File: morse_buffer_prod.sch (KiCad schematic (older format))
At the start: 105 parts, among them J1 Columns, J2 EXT_SW, J3 Rows, J4 TRIG_OUT, J5 Barrel_Jack_Switch, K1 G5V-1, Q1 MMBT2222A, Q2 MMBT2222A, Q3 NCE30P12S, Q4 MMBT2222A, SW1 M_RST, SW2 BTN, SW3 OUTPUT_SEL, U1 NE555D, U10 74HC138, U11 74HC138, U12 IDT7201LA50TP, U13 MORSE_EEPROM, U14 LENGTH_EEPROM, U15 74HC151, U16 74HC688, U17 74HC221, U18 74HC74, U19 74HC161, U2 NE555D, U20 74HC161, U21 PC817, U3 74HC32, U4 74HC32, U5 74HC14, U6 74HC10, U7 74HC74, U8 74HC74, U9 74HC161

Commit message: Add PS/2 controller
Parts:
- removed C21: 10nF, Capacitor_SMD:C_0603_1608Metric, symbol Device:C
- removed C22: 10uF, Capacitor_THT:CP_Radial_D5.0mm_P2.00mm, symbol Device:CP
- removed D1: TX/WAIT, LED_SMD:LED_0603_1608Metric, symbol Device:LED
- removed J1: Columns, Connector_PinHeader_2.54mm:PinHeader_1x13_P2.54mm_Vertical, symbol Connector:Screw_Terminal_01x13
- removed J3: Rows, Connector_PinHeader_2.54mm:PinHeader_1x04_P2.54mm_Vertical, symbol Connector:Screw_Terminal_01x04
- removed Q4: MMBT2222A, Package_TO_SOT_SMD:SOT-23, symbol Device:Q_NPN_BEC
- removed R11, R16, R21, R26, R27, R6, R7, R8, R9: 4K7, Resistor_SMD:R_0603_1608Metric, symbol Device:R
- removed R4: 1K, Resistor_SMD:R_0603_1608Metric, symbol Device:R
- removed U1: NE555D, Package_SO:SOIC-8_3.9x4.9mm_P1.27mm, symbol Timer:NE555D
- removed U10, U11: 74HC138, Package_SO:SOIC-16_3.9x9.9mm_P1.27mm, symbol 74xx:74LS138
- removed U3: 74HC32, Package_SO:SOIC-14_3.9x8.7mm_P1.27mm, symbol morse_ic:74HC32
- removed U7, U8: 74HC74, Package_SO:SOIC-14_3.9x8.7mm_P1.27mm, symbol 74xx:74HC74
- added J1: Keyboard, GiraffeTech-Connector:Connector_Mini-DIN_Female_6Pin_2rows, symbol Connector:Mini-DIN-6
- added R2: 4K7, Resistor_SMD:R_0603_1608Metric, symbol Device:R
- added R3: 1K, Resistor_SMD:R_0603_1608Metric, symbol Device:R
- added U1: 74HC74, Package_SO:SOIC-14_3.9x8.7mm_P1.27mm, symbol 74xx:74HC74
- added U10: 74HC280, Package_SO:SOIC-14_3.9x8.7mm_P1.27mm, symbol morse_ic:74HC280
- added U11: 74HC11, Package_SO:SOIC-14_3.9x8.7mm_P1.27mm, symbol morse_ic:74HC11
- added U3: 74HC14, Package_SO:SOIC-14_3.9x8.7mm_P1.27mm, symbol 74xx:74HC14
- added U7, U8: 74HC164, Package_SO:SOIC-14_3.9x8.7mm_P1.27mm, symbol 74xx:74HC164
- R1: value 470R -> 4K7
- renumbered R2 to R10, R15 to R11, R13 to R12, R22 to R13, R23 to R15, R17 to R16, R18 to R17, R19 to R18, R20 to R19, R24 to R4, R25 to R5, R3 to R6, R5 to R7, R12 to R8, R10 to R9
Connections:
- net +5V: now also J1.4, R2.1, U1.1 (~R), U1.10 (~S), U1.13 (~R), U1.14 (VCC), U10.14 (VCC), U11.14 (VCC), U3.14 (VCC), U7.14 (VCC), U7.9 (~MR), U8.14 (VCC), U8.9 (~MR); no longer U9.1 (~MR), U9.7 (CEP)
- net GNDREF: now also U5.1, U5.5, J1.3, U1.2 (D), U1.7 (GND), U10.7 (GND), U11.7 (GND), U3.13, U3.7 (GND), U7.7 (GND), U8.7 (GND)
- net KEYBOARD_PRESS: now also U11.12
- net RD_RESET: now also U3.1; no longer U4.1
- net TX_COMPLETE: now also U3.10; no longer Q2.3 (C)
- net TX_RESET: now also U5.3; no longer U6.1, U6.13, U6.2
- net ~FULL: now also U3.3; no longer U5.5
- net ~TX_RESET: now also U5.4; no longer U6.12
- net KBCLK: now reaches R1.2
- net KBCLK: now also Q2.3 (C), J1.5, U3.9
- net at U5.2: no longer U9.2 (CP)
- net at U19.2 (CP), U20.2 (CP): now also U3.6
- net at U2.3 (Q): now also U3.5
- net ~KB_INHIBIT: now reaches U4.3
- net ~KB_INHIBIT: now also U11.13; no longer U5.3
- net at U5.6: no longer U4.2
- net at U16.19 (P=R): now also U3.11
- net at Q2.1 (B): now also R3.1
- net COL_0: no longer names the net of U9.14 (Q0)
- net COL_0: now also U11.9; no longer U12.6 (D0)
- net COL_1: no longer names the net of U9.13 (Q1)
- net COL_1: now also U11.10; no longer U12.5 (D1)
- net COL_2: no longer names the net of U9.12 (Q2)
- net COL_2: no longer U12.4 (D2)
- net COL_3: no longer names the net of U9.11 (Q3)
- net COL_3: now also U11.11; no longer U12.3 (D3)
- net ROW_0 renamed KBD4
- net KBD4: now also U6.13, U10.12 (E), U7.11 (Q5)
- net ROW_1 renamed KBD5
- net KBD5: now also U10.11 (D), U11.5, U7.10 (Q4)
- net ROW_2 renamed KBD6
- net KBD6: now also U10.10 (C), U11.4, U7.6 (Q3)
- net ROW_3 renamed KBD7
- net KBD7: now also U10.9 (B), U11.3, U7.5 (Q2)
- new net: U11.6, U6.1, U6.2
- new net: U1.6 (~Q), U4.1
- new net: U1.8 (~Q), U4.2
- new net: U1.12 (D), U1.5 (Q)
- new net: R3.2, U3.4
- new net: U3.2, U9.1 (~MR), U9.7 (CEP)
- new net KBD0: U10.4 (I), U12.6 (D0), U8.4 (Q1)
- new net KBD1: U10.2 (H), U12.5 (D1), U8.3 (Q0)
- new net KBD2: U10.1 (G), U12.4 (D2), U7.13 (Q7), U8.1 (DSA), U8.2 (DSB)
- new net KBD3: U10.13 (F), U12.3 (D3), U7.12 (Q6)
- new net KBDAT: J1.1, R2.2, U7.1 (DSA), U7.2 (DSB)
- new net KBDP: U10.8 (A), U7.4 (Q1)
- new net KBD_END: U1.11 (C), U1.3 (C), U11.1, U11.8
- new net KBD_VALID: U10.6 (Odd), U11.2
- new net ~KBCLK: U3.8, U7.8 (CP), U8.8 (CP), U9.2 (CP)
- new net ~KB_BREAK: U1.4 (~S), U6.12
- no-connect marks 20 -> 28
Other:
- note added: "Break Code Detection"
- note added: "Break Code Inhibition State Machine"
- note added: "Comm Inhibit\non buffer full"
- note added: "Count 11 bits"
- note added: "Data Input Buffer"
- note added: "Device-To-Host data sequence:\n1 start bit (low)\n8 data bits (LSB first)\n1 parity bit (odd)\n1 stop bit (high)"
- note added: "FIFO Write Trigger"
- note added: "Invert clock signal\nfrom falling to rising"
- note added: "PS/2 Keyboard"
- note added: "Parity Check"
- note added: "Unused units"
- note removed: "Keyboard Scan (Col)"
- note removed: "Keyboard Scan (Row)"
- note removed: "Keyboard \nLock Reset"
- moved on the sheet: BZ1, C1, C10, C11, C12, C13, C14, C15, C16, C17, C18, C19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

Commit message: PCB routing
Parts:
- renumbered C8 to C1, C1 to C10, C7 to C11, C9 to C3, C10 to C7, C11 to C8, C3 to C9
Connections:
- net GNDREF: now also U3.1, U3.5, U5.3; no longer U3.13, U5.1, U5.5
- net KBCLK: now also U3.3; no longer U3.9
- net KBD0: now also U10.8 (A); no longer U10.4 (I)
- net KBD1: now also U10.9 (B); no longer U10.2 (H)
- net KBD5: now also U11.3; no longer U11.5
- net KBD7: now also U10.4 (I), U11.5; no longer U10.9 (B), U11.3
- net KBDP: now also U10.2 (H); no longer U10.8 (A)
- net KBD_END: now also U11.13; no longer U11.1
- net KBD_VALID: now also U11.1; no longer U11.2
- net RD_RESET: now also U5.5; no longer U3.1
- net TX_RESET: now also U5.1; no longer U5.3
- net ~FULL: now also U3.9; no longer U3.3
- net ~KBCLK: now also U3.4; no longer U3.8
- net ~KB_INHIBIT: now also U11.2; no longer U11.13
- net ~TX_RESET: now also U5.2; no longer U5.4
- net at U5.6: now also U9.1 (~MR), U9.7 (CEP)
- net at U2.3 (Q): now also U3.13; no longer U3.5
- net at U19.2 (CP), U20.2 (CP): now also U3.12; no longer U3.6
- net at R3.2: now also U3.8; no longer U3.4
- now unconnected: U3.2
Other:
- moved on the sheet: C1, C10, C11, C3, C7, C8, C9, U3A, U3B, U3C, U3D, U3F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

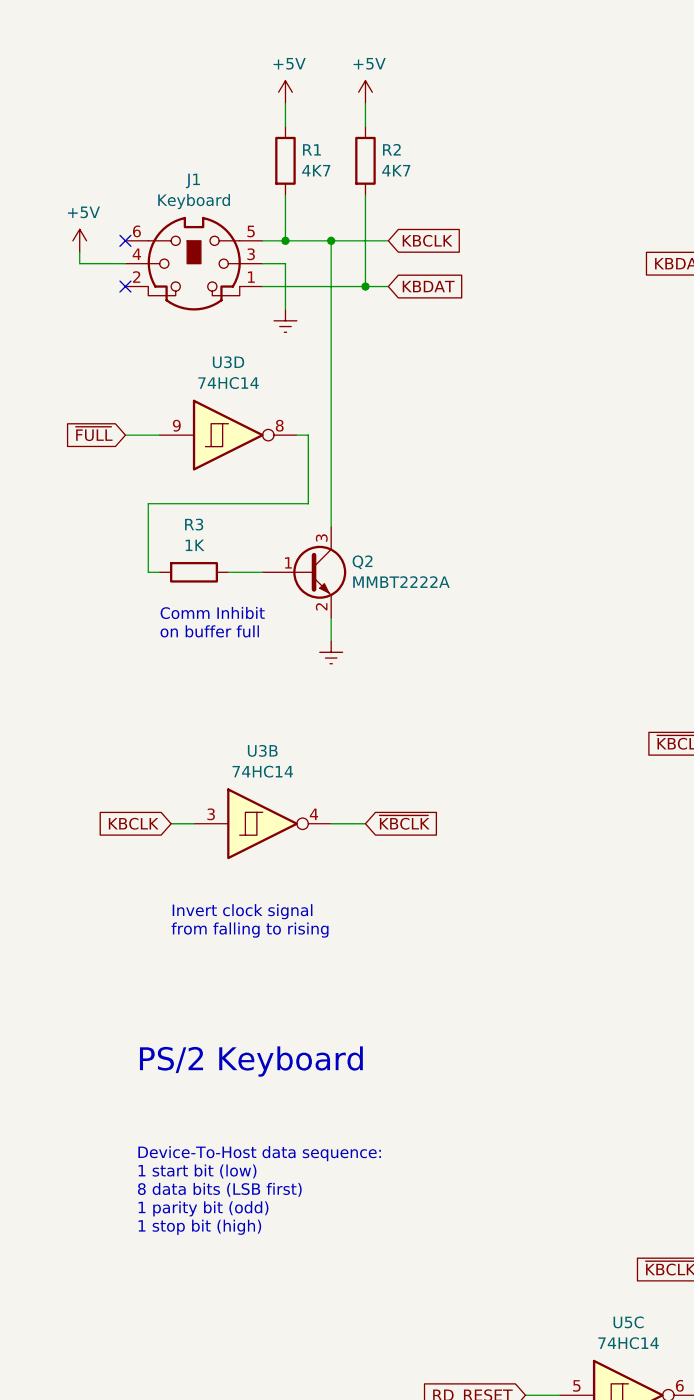
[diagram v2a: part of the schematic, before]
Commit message: Add fuse for ps/2 device
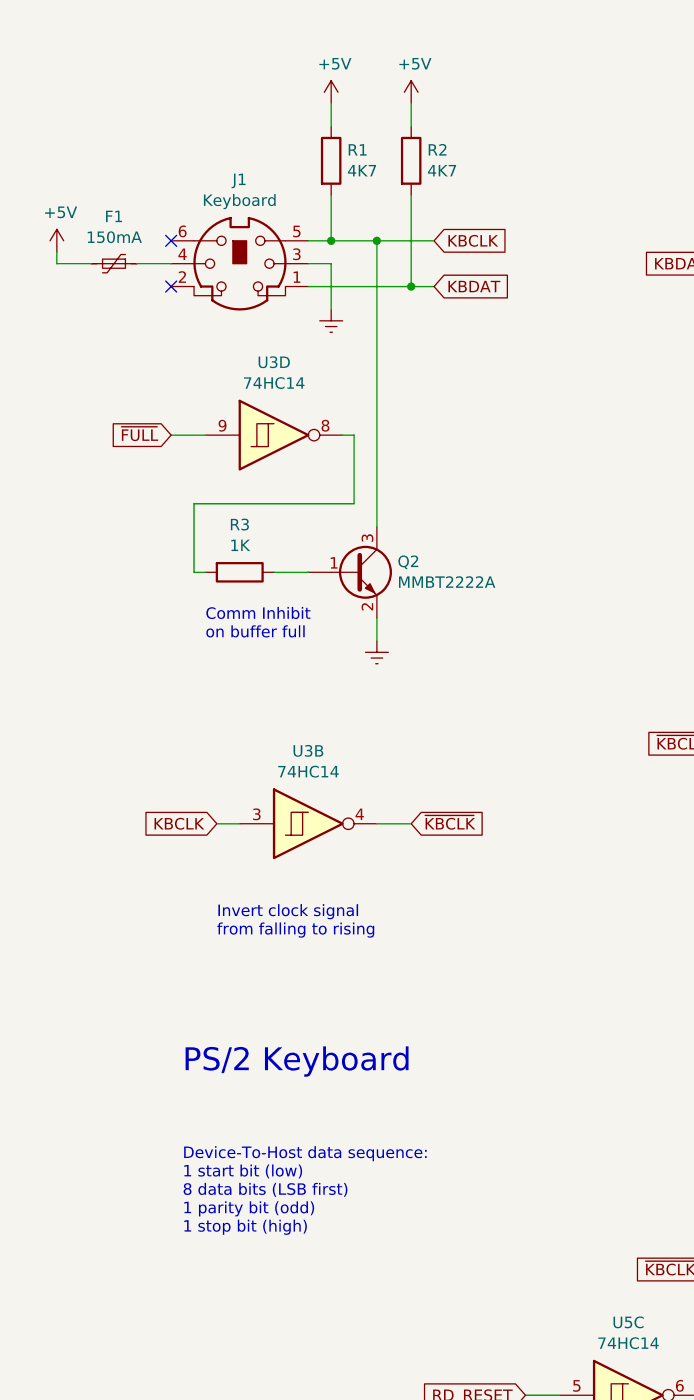
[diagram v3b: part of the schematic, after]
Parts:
- added F1: 150mA, Fuse:Fuse_1210_3225Metric, symbol Device:Polyfuse_Small
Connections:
- net +5V: now also F1.2; no longer J1.4
- new net: F1.1, J1.4
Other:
- moved on the sheet: J1, Q2, R1, R2, R3, U3B, U3D
